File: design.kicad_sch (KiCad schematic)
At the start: 163 parts, among them J301 TYPE-C-31-M-12, U1 TTP223, U10 ATtiny1616-M, U2 TTP223, U3 TTP223, U4 TTP223, U5 TTP223, U6 TTP223, U7 TTP223, U8 TTP223

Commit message: changed VCC to +5V and connect them
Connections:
- net VCC is gone; now on net +5V: C13.1, C14.1, C15.1, C16.1, C5.1, C6.1, C7.1, C8.1, JP1.2 (B), JP10.2 (B), JP11.2 (B), JP12.2 (B), JP13.2 (B), JP14.2 (B), JP15.2 (B), JP16.2 (B), JP2.2 (B), JP3.2 (B), JP4.2 (B), JP5.2 (B), JP6.2 (B), JP7.2 (B), JP8.2 (B), JP9.2 (B), U1.5 (VCC), U2.5 (VCC), U3.5 (VCC), U4.5 (VCC), U5.5 (VCC), U6.5 (VCC), U7.5 (VCC), U8.5 (VCC)
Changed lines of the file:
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@@
     (pin "1")
   )
-  (symbol (lib_id "power:VCC") (at 195.58 231.14 0) (unit 1)
+  (symbol (lib_id "power:+5V") (at 195.58 231.14 0) (unit 1)
     (in_bom yes) (on_board yes) (fields_autoplaced)
     (property "Reference" "#PWR033" (id 0) (at 195.58 234.95 0)
@@
     (pin "1")
   )
-  (symbol (lib_id "power:VCC") (at 103.505 231.775 0) (unit 1)
+  (symbol (lib_id "power:+5V") (at 103.505 231.775 0) (unit 1)
     (in_bom yes) (on_board yes) (fields_autoplaced)
     (property "Reference" "#PWR09" (id 0) (at 103.505 235.585 0)
@@
     (pin "1")
   )
-  (symbol (lib_id "power:VCC") (at 103.505 352.425 0) (unit 1)
+  (symbol (lib_id "power:+5V") (at 103.505 352.425 0) (unit 1)
     (in_bom yes) (on_board yes) (fields_autoplaced)
     (property "Reference" "#PWR012" (id 0) (at 103.505 356.235 0)
@@
     (pin "4")
   )
-  (symbol (lib_id "power:VCC") (at 103.505 271.145 0) (unit 1)
+  (symbol (lib_id "power:+5V") (at 103.505 271.145 0) (unit 1)
     (in_bom yes) (on_board yes) (fields_autoplaced)
     (property "Reference" "#PWR010" (id 0) (at 103.505 274.955 0)
@@
     (pin "2")
   )
-  (symbol (lib_id "power:VCC") (at 109.22 352.425 0) (unit 1)
+  (symbol (lib_id "power:+5V") (at 109.22 352.425 0) (unit 1)
     (in_bom yes) (on_board yes) (fields_autoplaced)
     (property "Reference" "#PWR019" (id 0) (at 109.22 356.235 0)
@@
     (pin "4")
   )
-  (symbol (lib_id "power:VCC") (at 109.22 231.775 0) (unit 1)
+  (symbol (lib_id "power:+5V") (at 109.22 231.775 0) (unit 1)
     (in_bom yes) (on_board yes) (fields_autoplaced)
     (property "Reference" "#PWR017" (id 0) (at 109.22 235.585 0)
@@
     (pin "2")
   )
-  (symbol (lib_id "power:VCC") (at 103.505 313.055 0) (unit 1)
+  (symbol (lib_id "power:+5V") (at 103.505 313.055 0) (unit 1)
     (in_bom yes) (on_board yes) (fields_autoplaced)
     (property "Reference" "#PWR011" (id 0) (at 103.505 316.865 0)
@@
     (pin "4")
   )
-  (symbol (lib_id "power:VCC") (at 190.5 351.79 0) (unit 1)
+  (symbol (lib_id "power:+5V") (at 190.5 351.79 0) (unit 1)
     (in_bom yes) (on_board yes) (fields_autoplaced)
     (property "Reference" "#PWR032" (id 0) (at 190.5 355.6 0)
@@
     (pin "1")
   )
-  (symbol (lib_id "power:VCC") (at 196.215 312.42 0) (unit 1)
+  (symbol (lib_id "power:+5V") (at 196.215 312.42 0) (unit 1)
     (in_bom yes) (on_board yes) (fields_autoplaced)
     (property "Reference" "#PWR037" (id 0) (at 196.215 316.23 0)
@@
     (pin "4")
   )
-  (symbol (lib_id "power:VCC") (at 196.215 270.51 0) (unit 1)
+  (symbol (lib_id "power:+5V") (at 196.215 270.51 0) (unit 1)
     (in_bom yes) (on_board yes) (fields_autoplaced)
     (property "Reference" "#PWR035" (id 0) (at 196.215 274.32 0)
@@
     (pin "4")
   )
-  (symbol (lib_id "power:VCC") (at 190.5 231.14 0) (unit 1)
+  (symbol (lib_id "power:+5V") (at 190.5 231.14 0) (unit 1)
     (in_bom yes) (on_board yes) (fields_autoplaced)
     (property "Reference" "#PWR029" (id 0) (at 190.5 234.95 0)
@@
     (pin "1")
   )
-  (symbol (lib_id "power:VCC") (at 108.585 313.055 0) (unit 1)
+  (symbol (lib_id "power:+5V") (at 108.585 313.055 0) (unit 1)
     (in_bom yes) (on_board yes) (fields_autoplaced)
     (property "Reference" "#PWR015" (id 0) (at 108.585 316.865 0)
@@
     (pin "1")
   )
-  (symbol (lib_id "power:VCC") (at 196.215 351.79 0) (unit 1)
+  (symbol (lib_id "power:+5V") (at 196.215 351.79 0) (unit 1)
     (in_bom yes) (on_board yes) (fields_autoplaced)
     (property "Reference" "#PWR039" (id 0) (at 196.215 355.6 0)
@@
     (pin "6")
   )
-  (symbol (lib_id "power:VCC") (at 190.5 312.42 0) (unit 1)
+  (symbol (lib_id "power:+5V") (at 190.5 312.42 0) (unit 1)
     (in_bom yes) (on_board yes) (fields_autoplaced)
     (property "Reference" "#PWR031" (id 0) (at 190.5 316.23 0)
@@
     (pin "1")
   )
-  (symbol (lib_id "power:VCC") (at 108.585 271.145 0) (unit 1)
+  (symbol (lib_id "power:+5V") (at 108.585 271.145 0) (unit 1)
     (in_bom yes) (on_board yes) (fields_autoplaced)
     (property "Reference" "#PWR013" (id 0) (at 108.585 274.955 0)
@@
     (pin "1")
   )
-  (symbol (lib_id "power:VCC") (at 190.5 270.51 0) (unit 1)
+  (symbol (lib_id "power:+5V") (at 190.5 270.51 0) (unit 1)
     (in_bom yes) (on_board yes) (fields_autoplaced)
     (property "Reference" "#PWR030" (id 0) (at 190.5 274.32 0)

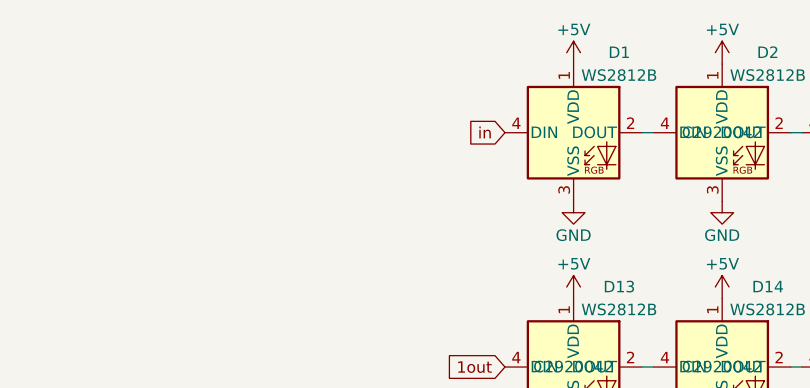
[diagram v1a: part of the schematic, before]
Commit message: add series resistor
closes #2
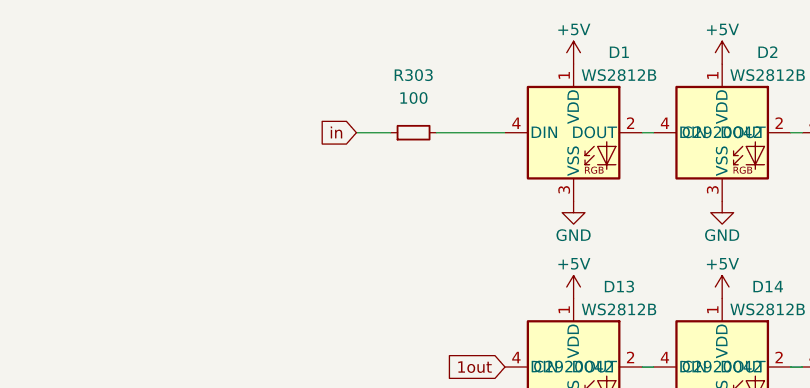
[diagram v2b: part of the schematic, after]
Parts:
- added R303: 100, Resistor_SMD:R_0805_2012Metric, symbol Device:R_Small
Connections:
- net in: now also R303.1; no longer D1.4 (DIN)
- new net: D1.4 (DIN), R303.2
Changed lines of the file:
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@@
     (stroke (width 0) (type default) (color 0 0 0 0))
   )
+  (wire (pts (xy 345.44 41.91) (xy 349.25 41.91))
+    (stroke (width 0) (type default) (color 0 0 0 0))
+  )
   (wire (pts (xy 349.885 289.56) (xy 349.885 288.29))
     (stroke (width 0) (type default) (color 0 0 0 0))
@@
     (stroke (width 0) (type default) (color 0 0 0 0))
   )
+  (wire (pts (xy 354.33 41.91) (xy 361.95 41.91))
+    (stroke (width 0) (type default) (color 0 0 0 0))
+  )
   (wire (pts (xy 185.42 320.04) (xy 190.5 320.04))
     (stroke (width 0) (type default) (color 0 0 0 0))
@@
     )
   )
-  (global_label "in" (shape input) (at 361.95 41.91 180) (fields_autoplaced)
+  (global_label "in" (shape input) (at 345.44 41.91 180) (fields_autoplaced)
     (effects (font (size 1.27 1.27)) (justify right))
-    (property "Referenzen zwischen Schaltplänen" "${INTERSHEET_REFS}" (id 0) (at 357.872 41.8306 0)
+    (property "Referenzen zwischen Schaltplänen" "${INTERSHEET_REFS}" (id 0) (at 341.362 41.8306 0)
       (effects (font (size 1.27 1.27)) (justify right) hide)
     )
@@
     (pin "1")
   )
+  (symbol (lib_id "Device:R_Small") (at 351.79 41.91 90) (unit 1)
+    (in_bom yes) (on_board yes) (fields_autoplaced)
+    (property "Reference" "R303" (id 0) (at 351.79 35.56 90))
+    (property "Value" "100" (id 1) (at 351.79 38.1 90))
+    (property "Footprint" "Resistor_SMD:R_0805_2012Metric" (id 2) (at 351.79 41.91 0)
+      (effects (font (size 1.27 1.27)) hide)
+    )
+    (property "Datasheet" "~" (id 3) (at 351.79 41.91 0)
+      (effects (font (size 1.27 1.27)) hide)
+    )
+    (pin "1")
+    (pin "2")
+  )
   (symbol (lib_id "power:GND") (at 468.63 180.34 0) (unit 1)
     (in_bom yes) (on_board yes)
@@
       (reference "R302") (unit 1) (value "5.1k") (footprint "Resistor_SMD:R_0805_2012Metric")
     )
+    (path "/11d7a6af-6ad4-40ba-a1bf-059102aa8773"
+      (reference "R303") (unit 1) (value "100") (footprint "Resistor_SMD:R_0805_2012Metric")
+    )
     (path "/c451642e-1278-4d6b-baa3-8abac3524fbe"
